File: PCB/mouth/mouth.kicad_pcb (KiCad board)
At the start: 2 copper layers, 60 x 50 mm, 61 parts, among them J1 Screw_Terminal_01x02, J2 Conn_01x04, J3 Conn_01x08, J5 Conn_02x08_Odd_Even, U1 RP2040, U2 W25Q32JVSS, U3 AP2112K-3.3, U4 74AHCT244, U5 74AHCT244, Y1 12MHz

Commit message: continue on mouth PCB
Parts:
- moved D1 174.4 mm to (26.9, 107.0)
- moved BOOT1 168.6 mm to (26.2, 94.0), turned to 90 degrees
- moved RUN1 158.8 mm to (38.6, 122.2)
- moved U1 154.4 mm to (33.2, 108.0)
- moved U2 154.0 mm to (33.2, 95.9)
- moved R3 152.5 mm to (25.2, 99.2), turned to -90 degrees
- moved R8 150.7 mm to (26.9, 108.6), turned to 180 degrees
- moved C1 146.6 mm to (29.1, 114.8), turned to 180 degrees
- moved R4 146.3 mm to (36.3, 114.6), turned to 180 degrees
- moved C3 143.9 mm to (32.7, 121.2), turned to 180 degrees
- moved R5 143.5 mm to (45.0, 128.8)
- moved C2 142.8 mm to (32.7, 116.0)
- moved R2 142.3 mm to (27.0, 99.2), turned to -90 degrees
- moved C11 142.0 mm to (26.9, 110.2)
- moved C10 141.4 mm to (26.9, 105.4)
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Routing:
- net GND: track 0.00 -> 201.1 mm, vias 0 -> 13
- net +3.3V: track 0.00 -> 102.0 mm, vias 0 -> 11
- net +5V: track 0.00 -> 84.1 mm, vias 0 -> 3
- net OE: track 0.00 -> 35.1 mm
- net R2: track 0.00 -> 30.4 mm
- net B1: track 0.00 -> 28.5 mm, vias 0 -> 1
- net LAT: track 0.00 -> 27.5 mm
- net R1: track 0.00 -> 25.1 mm, vias 0 -> 1
- net G1: track 0.00 -> 24.8 mm, vias 0 -> 1
- net +1V1: track 0.00 -> 21.9 mm, vias 0 -> 3
- net /QSPI_SS: track 0.00 -> 15.1 mm
- net /QSPI_SD3: track 0.00 -> 14.3 mm
- net RUN: track 0.00 -> 14.1 mm
- net CLK: track 0.00 -> 14.1 mm
- net /QSPI_SCLK: track 0.00 -> 12.9 mm
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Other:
- board size 60 x 50 mm -> 49.6 x 50 mm

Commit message: more pcb
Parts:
- moved RUN1 0.71 mm to (37.9, 122.1)
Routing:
- net SWDIO: track 0.00 -> 104.4 mm, vias 0 -> 2
- net SWCLK: track 0.00 -> 96.8 mm, vias 0 -> 3
- net RUN: track 14.1 -> 104.3 mm, vias 0 -> 1
- net TX: track 2.74 -> 71.7 mm, vias 1 -> 2
- net PIN_C: track 2.64 -> 68.2 mm
- net RX: track 1.24 -> 66.5 mm, vias 1 -> 2
- net GND: track 201.1 -> 261.7 mm, vias 13 -> 23
- net PIN_D: track 1.65 -> 60.2 mm, vias 1 -> 2
- net PIN_OE: track 1.62 -> 58.7 mm, vias 1 -> 4
- net PIN_CLK: track 1.30 -> 57.2 mm, vias 1 -> 2
- net PIN_R2: track 3.09 -> 51.9 mm, vias 2 -> 6
- net PIN_LAT: track 1.45 -> 49.8 mm, vias 1 -> 4
- net PIN_B: track 4.31 -> 48.3 mm, vias 2 -> 4
- net PIN_B2: track 2.52 -> 45.4 mm, vias 2 -> 4
- net PIN_E: track 3.06 -> 45.3 mm
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
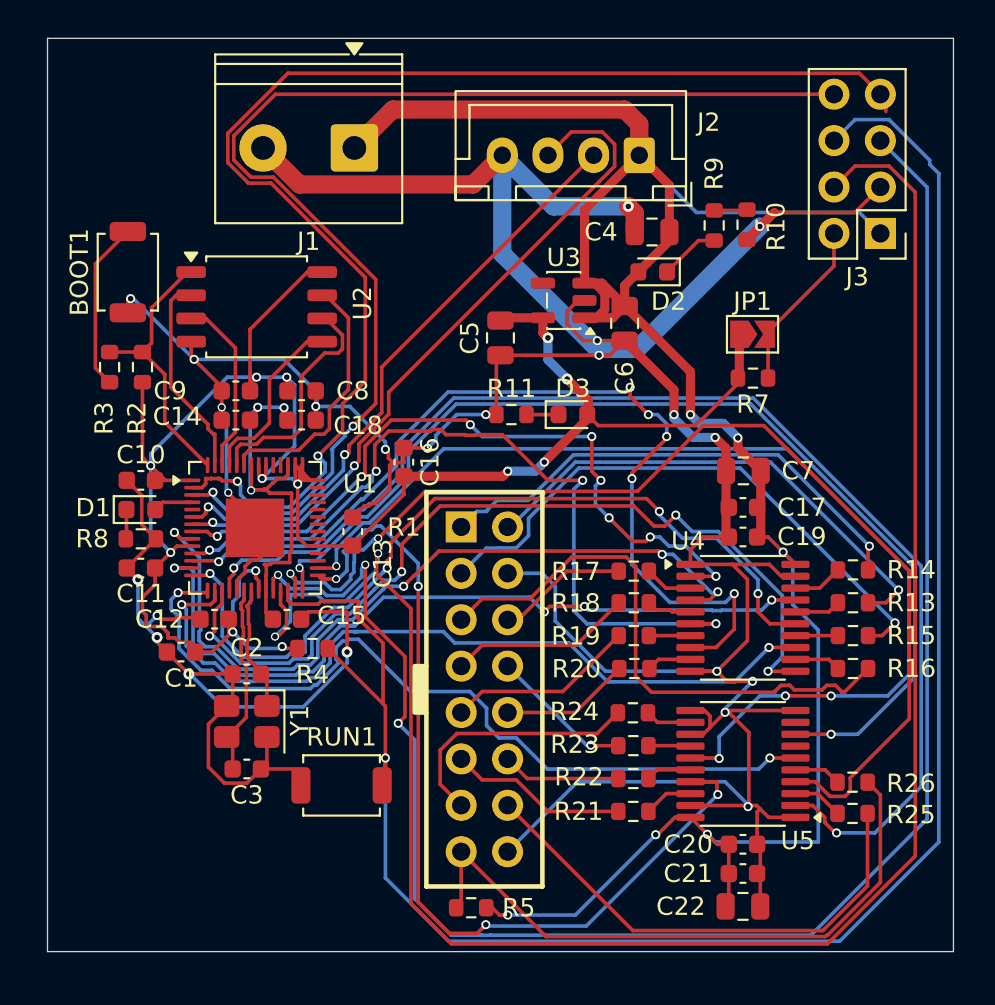
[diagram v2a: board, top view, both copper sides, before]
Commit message: finish mouth pcb
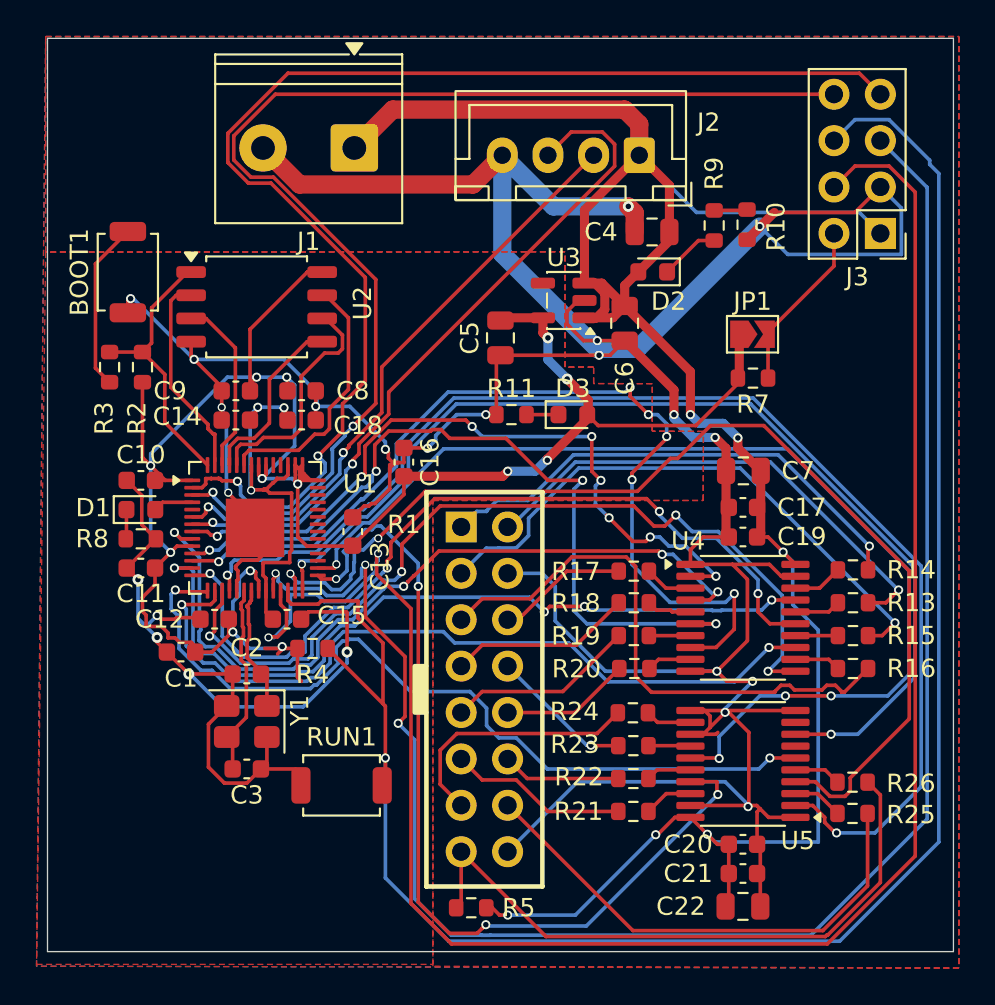
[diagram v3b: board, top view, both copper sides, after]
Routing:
- net GND: track 261.7 -> 278.1 mm
- net +3.3V: track 115.9 -> 119.7 mm
- net SWDIO: track 104.4 -> 105.3 mm
- net TX: track 71.7 -> 71.0 mm
- net SWCLK: track 96.8 -> 97.4 mm
- added copper zone on F.Cu, net +3.3V
- added copper zone on F.Cu, net +5V
- added copper zone on B.Cu, net GND
- added copper zone on F.Cu, net GND
